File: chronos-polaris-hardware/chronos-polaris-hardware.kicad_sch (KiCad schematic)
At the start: 61 parts, among them J1 Conn_01x03_Pin, J2 Conn_01x03_Pin, J3 Conn_01x03_Pin, J4 Conn_01x03_Pin, J5 Conn_01x03_Pin, J6 Conn_01x04, J7 Conn_01x04, J8 Conn_01x02, P1 WJ124-3_81-6P, U1 TPS62172DSGR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

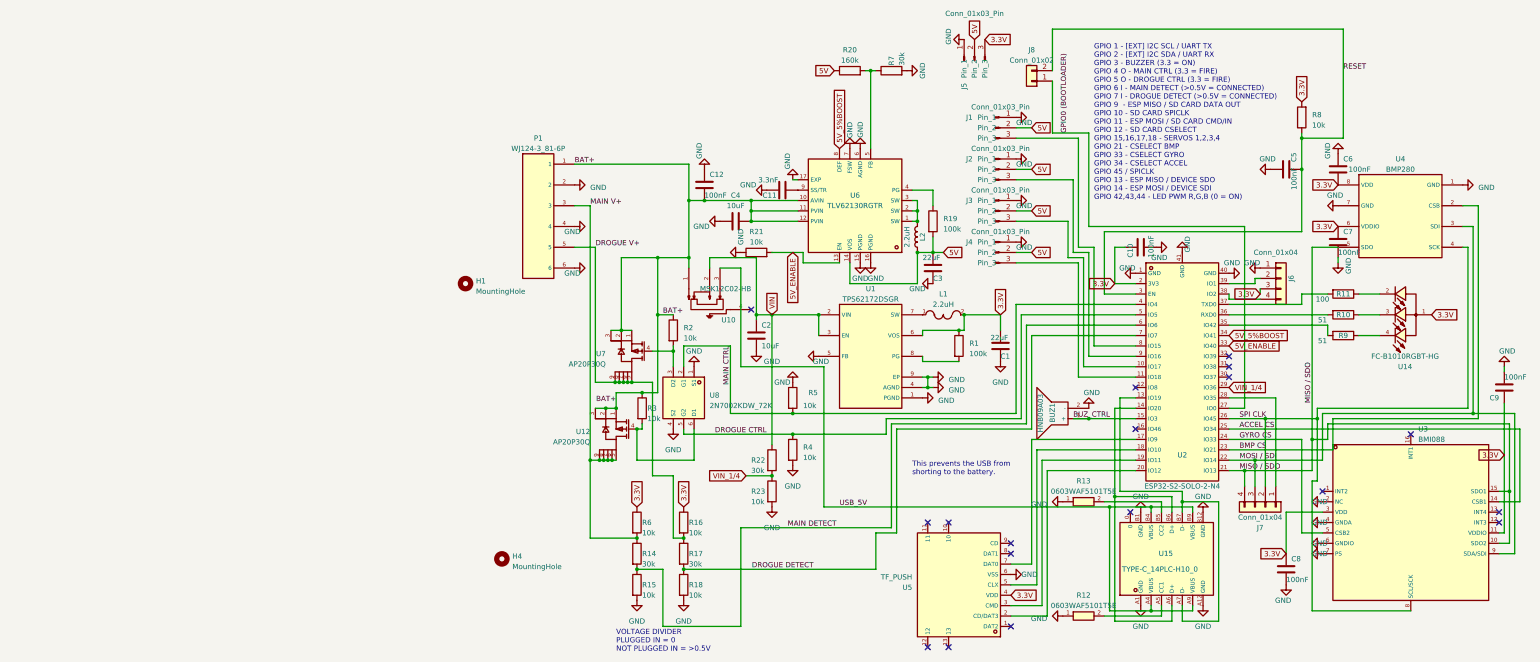
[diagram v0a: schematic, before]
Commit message: Cleaned up Pressure Sensor and StepDownConverter. - Rishik B.
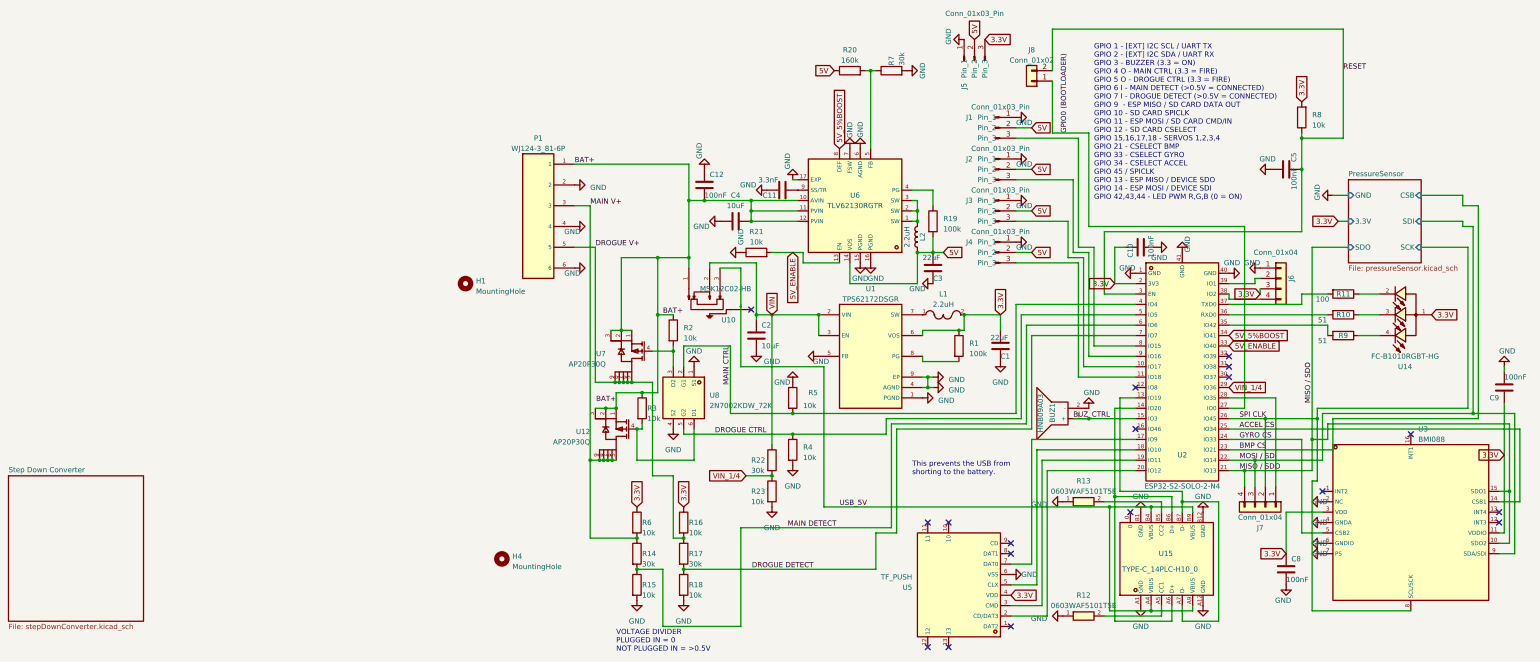
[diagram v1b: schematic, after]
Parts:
- removed C6, C7: 100nF, Capacitor_SMD:C_0402_1005Metric, symbol Device:C
- removed U4: BMP280, polaris-fp:LGA-8_L2.5-W2.0-P0.65_AMP6127, symbol polaris-sym:BMP280
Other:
- added sheet PressureSensor (pressureSensor.kicad_sch)
- added sheet Step Down Converter (stepDownConverter.kicad_sch)

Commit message: changed label names. - Rishik B.
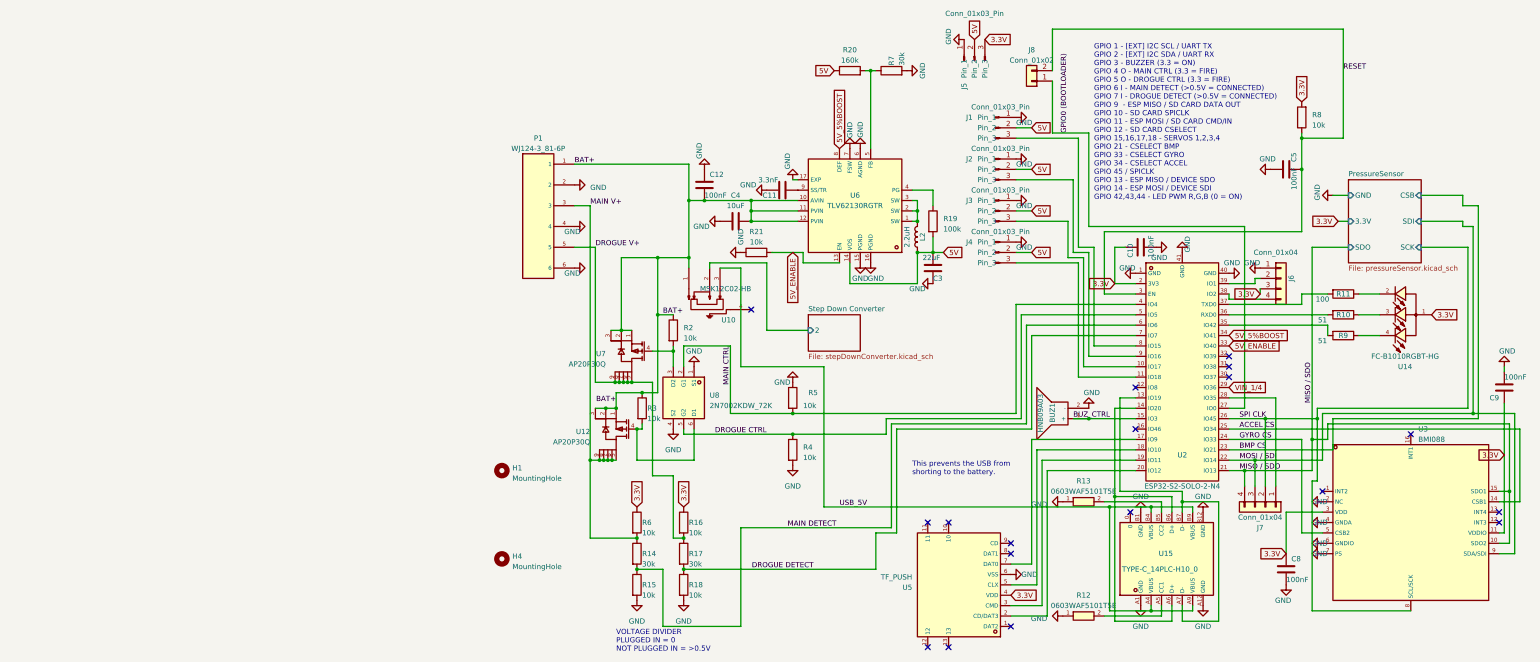
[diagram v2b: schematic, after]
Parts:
- removed C1: 22uF, Capacitor_SMD:C_0603_1608Metric, symbol Device:C
- removed C2: 10uF, Capacitor_SMD:C_0805_2012Metric, symbol Device:C
- removed L1: 2.2uH, polaris-fp:IND-SMD_L3.0-W3.0, symbol polaris-sym:SWPA3015S2R2MT
- removed R1: 100k, Resistor_SMD:R_0603_1608Metric, symbol Device:R
- removed R22: 30k, Resistor_SMD:R_0603_1608Metric, symbol Device:R
- removed R23: 10k, Resistor_SMD:R_0603_1608Metric, symbol Device:R
- removed U1: TPS62172DSGR, polaris-fp:WSON-8_L2.0-W2.0-P0.50-TL-EP, symbol polaris-sym:TPS62172DSGR
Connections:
- net VIN renamed Step Down Converter/2
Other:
- sheet Step Down Converter ports: added 2; removed none
- moved on the sheet: H1

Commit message: combined jazeb changes into mine. - Rishik B.
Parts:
- removed C11: 3.3nF, Capacitor_SMD:C_0402_1005Metric, symbol Device:C
- removed C12: 100nF, Capacitor_SMD:C_0402_1005Metric, symbol Device:C
- removed C3: 22uF, Capacitor_SMD:C_0603_1608Metric, symbol Device:C
- removed C4: 10uF, Capacitor_SMD:C_0805_2012Metric, symbol Device:C
- removed L2: 2.2uH, polaris-fp:IND-SMD_L4.0-W4.0, symbol Device:L
- removed R19: 100k, Resistor_SMD:R_0603_1608Metric, symbol Device:R
- removed R20: 160k, Resistor_SMD:R_0603_1608Metric, symbol Device:R
- removed R21: 10k, Resistor_SMD:R_0603_1608Metric, symbol Device:R
- removed R7: 30k, Resistor_SMD:R_0603_1608Metric, symbol Device:R
- removed U6: TLV62130RGTR, polaris-fp:QFN-16_L3.0-W3.0-P0.50-TL-EP, symbol polaris-sym:TLV62130RGTR
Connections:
- net Step Down Converter/2 renamed Step Down Converter/unknown2
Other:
- added sheet Switching Voltage Regulator (switchingVoltageRegulator.kicad_sch)
- sheet Step Down Converter ports: added unknown2; removed 2

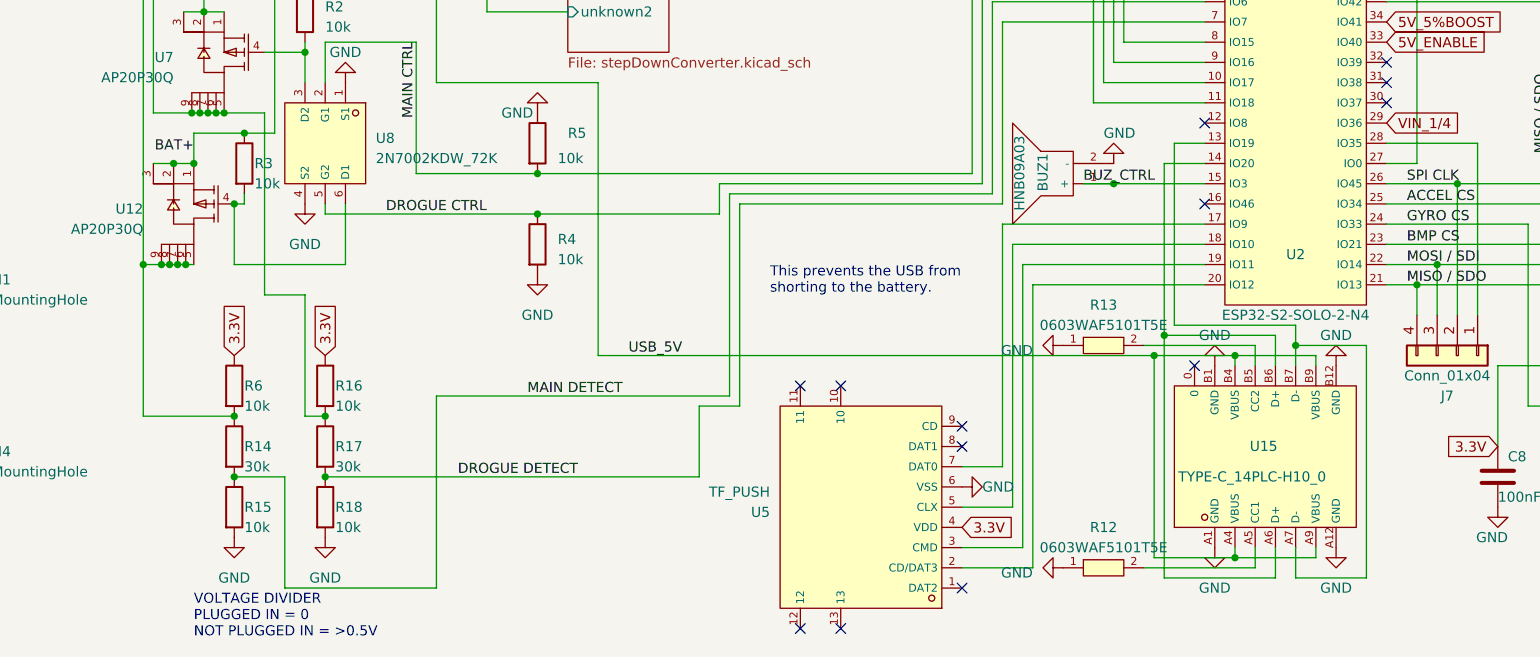
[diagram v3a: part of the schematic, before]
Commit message: Added Type C. Need to integrate Dual-PNP-Small-Signal-Transistor.kicad_sch
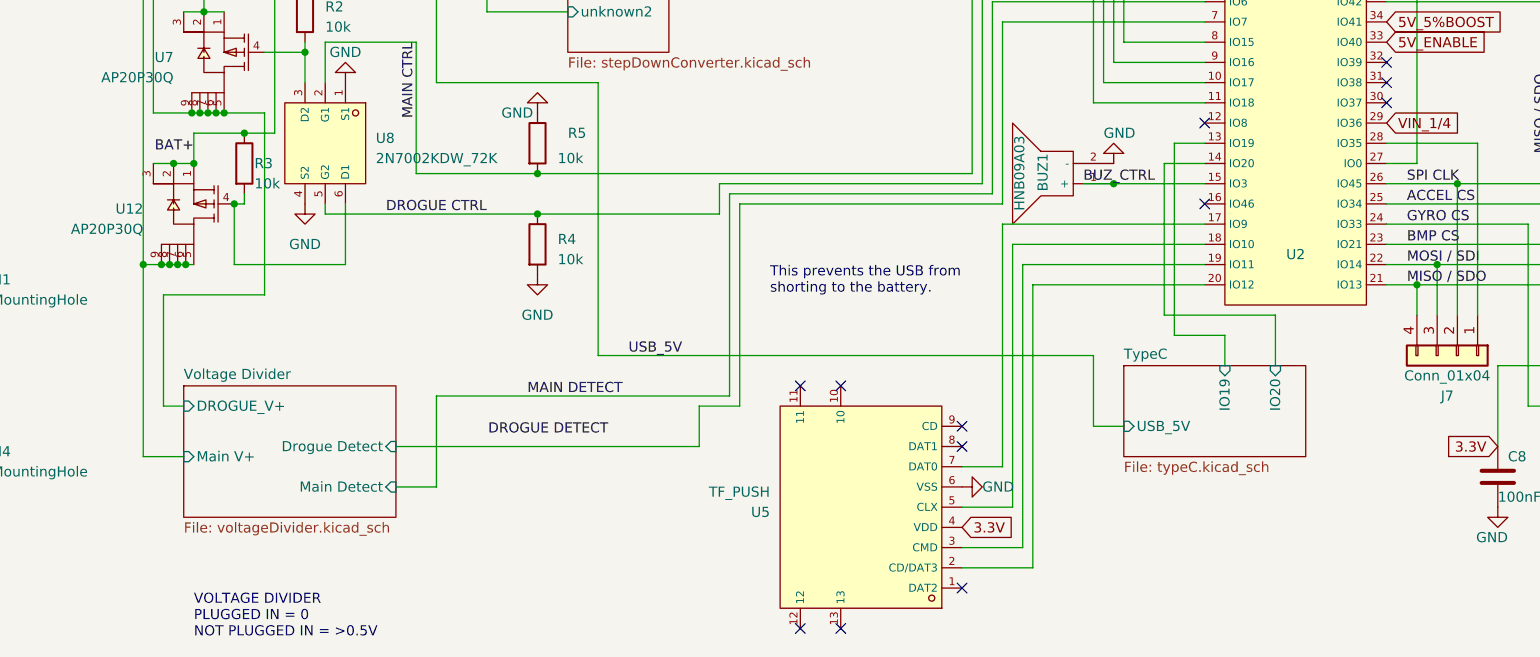
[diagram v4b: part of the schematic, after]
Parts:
- removed R12, R13: 0603WAF5101T5E, polaris-fp:R0603, symbol polaris-sym:0603WAF5101T5E
- removed R14, R17: 30k, Resistor_SMD:R_0603_1608Metric, symbol Device:R
- removed R15, R16, R18, R6: 10k, Resistor_SMD:R_0603_1608Metric, symbol Device:R
- removed U15: TYPE-C_14PLC-H10_0, polaris-fp:USB-C-TH_SHOUHAN_TYPE-C-14PLC-H10.0, symbol polaris-sym:TYPE-C_14PLC-H10_0
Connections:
- net DROGUE DETECT: no longer U2.7 (IO7)
- net TypeC/IO19: now reaches U2.13 (IO19)
- net TypeC/IO20: now reaches U2.14 (IO20)
- new net Voltage Divider/Drogue Detect: U2.7 (IO7)
- no-connect marks 18 -> 17
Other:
- added sheet TypeC (typeC.kicad_sch)
- added sheet Voltage Divider (voltageDivider.kicad_sch)

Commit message: asdf
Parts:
- removed R2, R3, R4, R5: 10k, Resistor_SMD:R_0603_1608Metric, symbol Device:R
- removed U12, U7: AP20P30Q, polaris-fp:DFN-8_L3.3-W3.0-P0.65-LS3.3-BL-EP, symbol polaris-sym:AP20P30Q
- removed U8: 2N7002KDW_72K, polaris-fp:SOT-363_L2.1-W1.3-P0.65-LS2.3-BL, symbol polaris-sym:2N7002KDW_72K
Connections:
- net DROGUE CTRL renamed Dual-PNP-Small-Signal-Transistor/pin IO5
- net MAIN CTRL renamed Dual-PNP-Small-Signal-Transistor/pin IO4
- net Step Down Converter to 3.3V/unknown2 renamed Step Down Converter to 3.3V/VIN
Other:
- sheet Step Down Converter renamed Step Down Converter to 3.3V
- added sheet Dual-PNP-Small-Signal-Transistor (Dual-PNP-Small-Signal-Transistor_sch.kicad_sch)
- sheet Step Down Converter to 3.3V ports: added VIN; removed unknown2
- sheet Switching Voltage Regulator ports: added BAT+; removed unknown1

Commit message: made satvik fixes
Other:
- sheet Step Down Converter to 3.3V ports: added 3.3V, VIN_1/4; removed none
- sheet Switching Voltage Regulator ports: added 5V, 5V_5%BOOST; removed none
- sheet Voltage Divider ports: added 3.3V; removed none
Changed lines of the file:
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@@
 	(wire
 		(pts
+			(xy 123.19 93.98) (xy 127 93.98)
+		)
+		(stroke
+			(width 0)
+			(type default)
+		)
+	)
+	(wire
+		(pts
 			(xy 93.98 142.24) (xy 130.81 142.24)
 		)
@@
 	(wire
 		(pts
+			(xy 92.71 62.23) (xy 96.52 62.23)
+		)
+		(stroke
+			(width 0)
+			(type default)
+		)
+	)
+	(wire
+		(pts
 			(xy 165.1 64.77) (xy 161.29 64.77)
 		)
@@
 	(wire
 		(pts
+			(xy 59.69 154.94) (xy 62.23 154.94)
+		)
+		(stroke
+			(width 0)
+			(type default)
+		)
+	)
+	(wire
+		(pts
 			(xy 53.34 73.66) (xy 58.42 73.66)
 		)
@@
 	(wire
 		(pts
+			(xy 91.44 64.77) (xy 96.52 64.77)
+		)
+		(stroke
+			(width 0)
+			(type default)
+		)
+	)
+	(wire
+		(pts
 			(xy 53.34 63.5) (xy 57.15 63.5)
 		)
@@
 	(wire
 		(pts
+			(xy 107.95 96.52) (xy 110.49 96.52)
+		)
+		(stroke
+			(width 0)
+			(type default)
+		)
+	)
+	(wire
+		(pts
 			(xy 180.34 97.79) (xy 190.5 97.79)
 		)
@@
 		)
 	)
+	(global_label "3.3V"
+		(shape input)
+		(at 59.69 154.94 180)
+		(fields_autoplaced yes)
+		(effects
+			(font
+				(size 1.27 1.27)
+			)
+			(justify right)
+		)
+		(property "Intersheetrefs" "${INTERSHEET_REFS}"
+			(at 52.5924 154.94 0)
+			(effects
+				(font
+					(size 1.27 1.27)
+				)
+				(justify right)
+				(hide yes)
+			)
+		)
+	)
+	(global_label "3.3V"
+		(shape input)
+		(at 127 93.98 0)
+		(fields_autoplaced yes)
+		(effects
+			(font
+				(size 1.27 1.27)
+			)
+			(justify left)
+		)
+		(property "Intersheetrefs" "${INTERSHEET_REFS}"
+			(at 134.0976 93.98 0)
+			(effects
+				(font
+					(size 1.27 1.27)
+				)
+				(justify left)
+				(hide yes)
+			)
+		)
+	)
 	(global_label "5V"
 		(shape input)
@@
 	(global_label "5V"
 		(shape input)
+		(at 92.71 62.23 180)
+		(fields_autoplaced yes)
+		(effects
+			(font
+				(size 1.27 1.27)
+			)
+			(justify right)
+		)
+		(property "Intersheetrefs" "${INTERSHEET_REFS}"
+			(at 87.4267 62.23 0)
+			(effects
+				(font
+					(size 1.27 1.27)
+				)
+				(justify right)
+				(hide yes)
+			)
+		)
+	)
+	(global_label "5V"
+		(shape input)
 		(at 165.1 54.61 0)
 		(fields_autoplaced yes)
@@
 		)
 	)
+	(global_label "VIN_1{slash}4"
+		(shape input)
+		(at 107.95 96.52 180)
+		(fields_autoplaced yes)
+		(effects
+			(font
+				(size 1.27 1.27)
+			)
+			(justify right)
+		)
+		(property "Intersheetrefs" "${INTERSHEET_REFS}"
+			(at 97.2238 96.52 0)
+			(effects
+				(font
+					(size 1.27 1.27)
+				)
+				(justify right)
+				(hide yes)
+			)
+		)
+	)
 	(global_label "3.3V"
 		(shape input)
@@
 	(global_label "5V_5%BOOST"
 		(shape input)
+		(at 91.44 64.77 180)
+		(fields_autoplaced yes)
+		(effects
+			(font
+				(size 1.27 1.27)
+			)
+			(justify right)
+		)
+		(property "Intersheetrefs" "${INTERSHEET_REFS}"
+			(at 76.4201 64.77 0)
+			(effects
+				(font
+					(size 1.27 1.27)
+				)
+				(justify right)
+				(hide yes)
+			)
+		)
+	)
+	(global_label "5V_5%BOOST"
+		(shape input)
 		(at 213.36 95.25 0)
 		(fields_autoplaced yes)
@@
 			)
 		)
+		(pin "VIN_1{slash}4" input
+			(at 110.49 96.52 180)
+			(effects
+				(font
+					(size 1.27 1.27)
+				)
+				(justify left)
+			)
+		)
+		(pin "3.3V" input
+			(at 123.19 93.98 0)
+			(effects
+				(font
+					(size 1.27 1.27)
+				)
+				(justify right)
+			)
+		)
 		(instances
 			(project "chronos-polaris-hardware"
@@
 	(sheet
 		(at 96.52 55.88)
-		(size 25.4 8.89)
+		(size 25.4 12.7)
 		(fields_autoplaced yes)
 		(stroke
@@
 		)
 		(property "Sheetfile" "switchingVoltageRegulator.kicad_sch"
-			(at 96.52 65.3546 0)
+			(at 96.52 69.1646 0)
 			(effects
 				(font
@@
 			)
 		)
+		(pin "5V" input
+			(at 96.52 62.23 180)
+			(effects
+				(font
+					(size 1.27 1.27)
+				)
+				(justify left)
+			)
+		)
+		(pin "5V_5%BOOST" input
+			(at 96.52 64.77 180)
+			(effects
+				(font
+					(size 1.27 1.27)
+				)
+				(justify left)
+			)
+		)
 		(instances
 			(project "chronos-polaris-hardware"
@@
 			(effects
 				(font
+					(size 1.27 1.27)
+				)
+				(justify left)
+			)
+		)
+		(pin "3.3V" input
+			(at 62.23 154.94 180)
+			(effects
+				(font

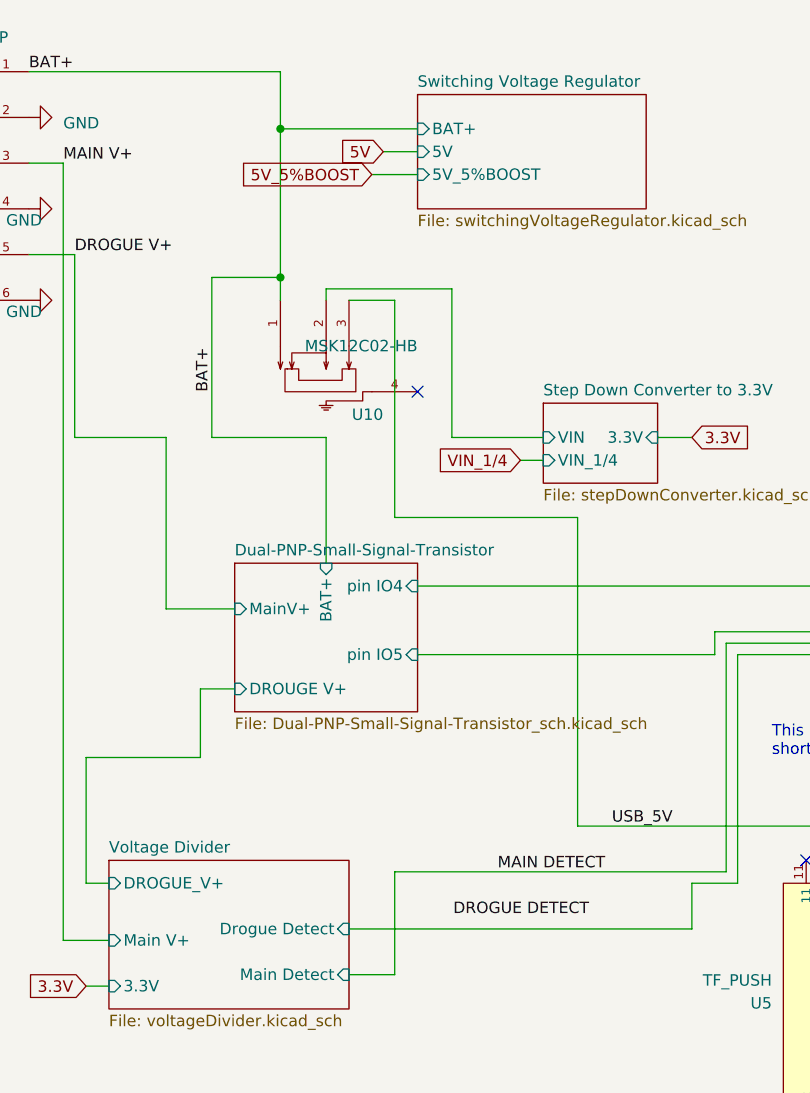
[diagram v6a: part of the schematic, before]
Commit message: Update chronos-polaris-hardware.kicad_sch
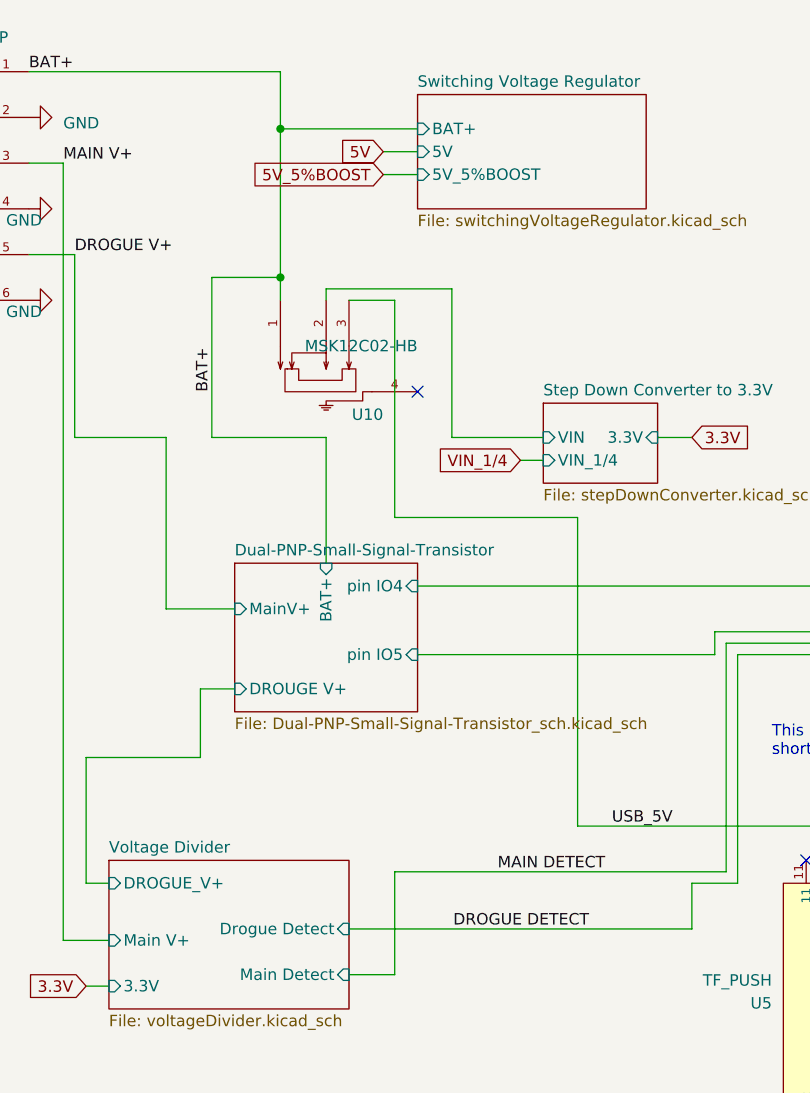
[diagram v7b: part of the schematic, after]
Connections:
- net Voltage Divider/Drogue Detect is gone; now on net DROGUE DETECT: U2.7 (IO7)
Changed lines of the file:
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@@
 	(wire
 		(pts
-			(xy 91.44 64.77) (xy 96.52 64.77)
+			(xy 92.71 64.77) (xy 96.52 64.77)
 		)
 		(stroke
@@
 	)
 	(label "DROGUE DETECT"
-		(at 115.57 147.32 180)
+		(at 115.57 148.59 180)
 		(fields_autoplaced yes)
 		(effects
@@
 	(global_label "5V_5%BOOST"
 		(shape input)
-		(at 91.44 64.77 180)
+		(at 92.71 64.77 180)
 		(fields_autoplaced yes)
 		(effects
@@
 		)
 		(property "Intersheetrefs" "${INTERSHEET_REFS}"
-			(at 76.4201 64.77 0)
-			(effects
-				(font
+			(at 77.6901 64.77 0)
+			(effects
+				(font
